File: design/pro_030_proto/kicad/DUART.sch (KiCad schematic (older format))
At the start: 1 part, among them U9 XR68C681CJTR-F-XR68C681

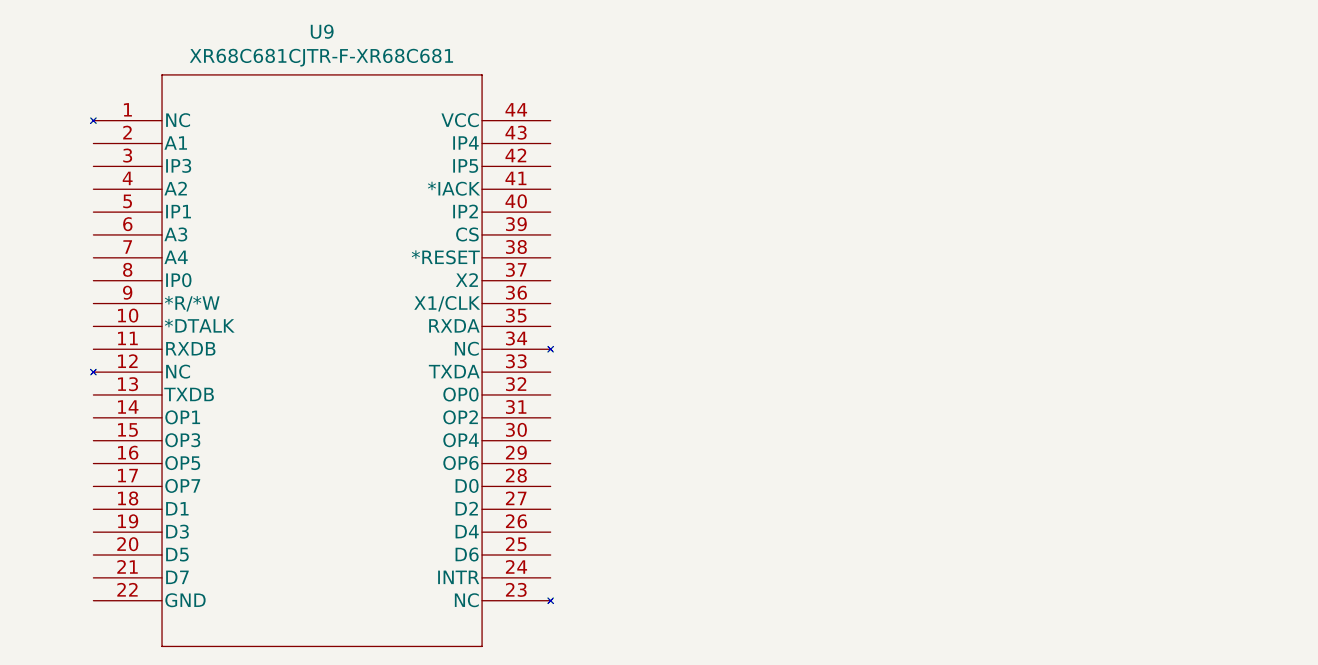
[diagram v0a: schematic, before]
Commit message: Add interrupt glue to schematic
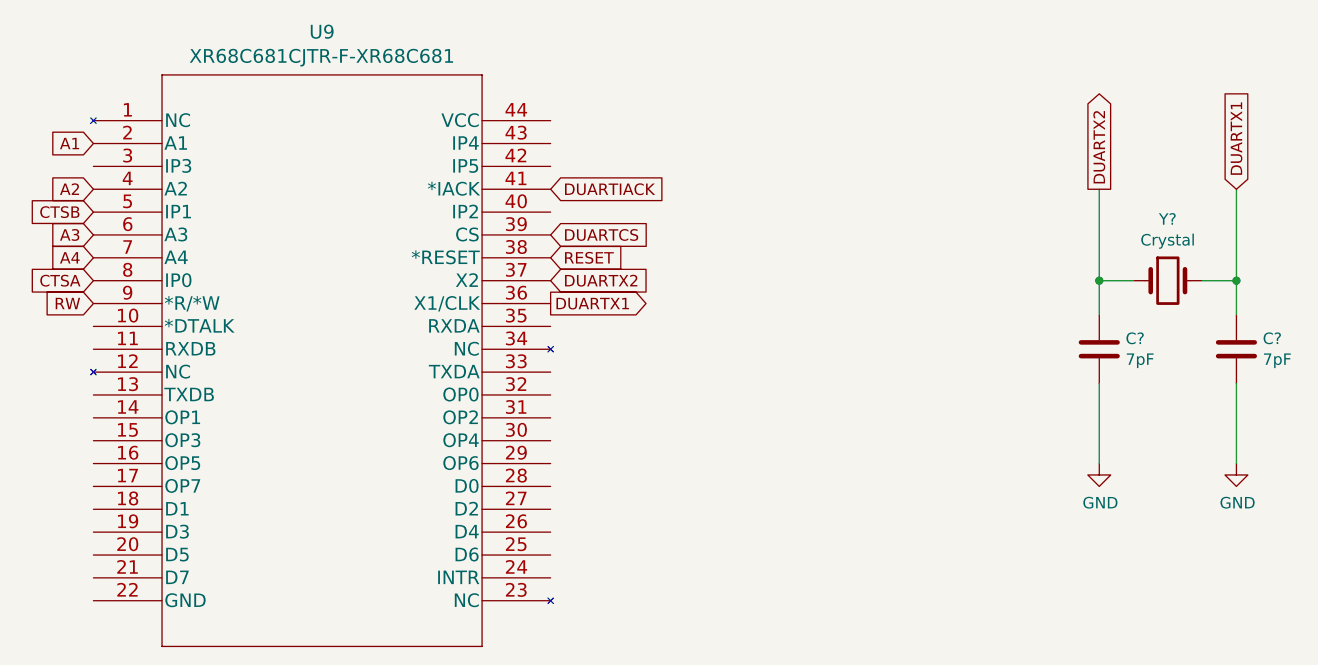
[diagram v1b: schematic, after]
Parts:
- added C? (x2): 7pF, Capacitor_THT:C_Rect_L4.0mm_W2.5mm_P2.50mm, symbol Device:C
- added Y?: Crystal, symbol Device:Crystal
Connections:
- net A1: now reaches U9.2 (A1)
- net DUARTX1: now reaches U9.36 (X1/CLK)
- net DUARTX1: now also C?.1, Y?.2
- net DUARTX2: now reaches U9.37 (X2)
- net DUARTX2: now also C?.1, Y?.1
- net RESET: now reaches U9.38 (*RESET)
- net DUARTCS: now reaches U9.39 (CS)
- net A2: now reaches U9.4 (A2)
- net DUARTIACK: now reaches U9.41 (*IACK)
- net CTSB: now reaches U9.5 (IP1)
- net A3: now reaches U9.6 (A3)
- net A4: now reaches U9.7 (A4)
- net CTSA: now reaches U9.8 (IP0)
- net RW: now reaches U9.9 (*R/*W)
- new net GND: C?.2, C?.2
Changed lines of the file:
@@
 $Descr A4 11693 8268
 encoding utf-8
-Sheet 5 7
+Sheet 5 8
 Title "rosco_m68k Pro (030) Prototype"
 Date "2021-07-16"
@@
 	1    0    0    -1
 $EndComp
+$Comp
+L Device:Crystal Y?
+U 1 1 60FCCD46
+P 7800 3450
+F 0 "Y?" H 7800 3718 50  0000 C CNN
+F 1 "Crystal" H 7800 3627 50  0000 C CNN
+F 2 "" H 7800 3450 50  0001 C CNN
+F 3 "~" H 7800 3450 50  0001 C CNN
+	1    7800 3450
+	1    0    0    -1
+$EndComp
+Text GLabel 5100 3450 2    50   Input ~ 0
+DUARTX2
+Text GLabel 5100 3550 2    50   Output ~ 0
+DUARTX1
+Text GLabel 7500 3050 1    50   Output ~ 0
+DUARTX2
+Text GLabel 8100 3050 1    50   Input ~ 0
+DUARTX1
+Wire Wire Line
+	7650 3450 7500 3450
+Wire Wire Line
+	7500 3450 7500 3050
+Wire Wire Line
+	7950 3450 8100 3450
+Wire Wire Line
+	8100 3450 8100 3050
+$Comp
+L Device:C C?
+U 1 1 60FD6D0D
+P 7500 3750
+AR Path="/60EC67C5/60FD6D0D" Ref="C?"  Part="1"
+AR Path="/60FBD3A8/60FD6D0D" Ref="C?"  Part="1"
+F 0 "C?" H 7615 3796 50  0000 L CNN
+F 1 "7pF" H 7615 3705 50  0000 L CNN
+F 2 "Capacitor_THT:C_Rect_L4.0mm_W2.5mm_P2.50mm" H 7538 3600 50  0001 C CNN
+F 3 "~" H 7500 3750 50  0001 C CNN
+	1    7500 3750
+	1    0    0    -1
+$EndComp
+$Comp
+L Device:C C?
+U 1 1 60FD71CD
+P 8100 3750
+AR Path="/60EC67C5/60FD71CD" Ref="C?"  Part="1"
+AR Path="/60FBD3A8/60FD71CD" Ref="C?"  Part="1"
+F 0 "C?" H 8215 3796 50  0000 L CNN
+F 1 "7pF" H 8215 3705 50  0000 L CNN
+F 2 "Capacitor_THT:C_Rect_L4.0mm_W2.5mm_P2.50mm" H 8138 3600 50  0001 C CNN
+F 3 "~" H 8100 3750 50  0001 C CNN
+	1    8100 3750
+	1    0    0    -1
+$EndComp
+Wire Wire Line
+	7500 3450 7500 3600
+Connection ~ 7500 3450
+Wire Wire Line
+	8100 3450 8100 3600
+Connection ~ 8100 3450
+$Comp
+L power:GND #PWR?
+U 1 1 60FD7528
+P 7500 4250
+F 0 "#PWR?" H 7500 4000 50  0001 C CNN
+F 1 "GND" H 7505 4077 50  0000 C CNN
+F 2 "" H 7500 4250 50  0001 C CNN
+F 3 "" H 7500 4250 50  0001 C CNN
+	1    7500 4250
+	1    0    0    -1
+$EndComp
+$Comp
+L power:GND #PWR?
+U 1 1 60FD7E93
+P 8100 4250
+F 0 "#PWR?" H 8100 4000 50  0001 C CNN
+F 1 "GND" H 8105 4077 50  0000 C CNN
+F 2 "" H 8100 4250 50  0001 C CNN
+F 3 "" H 8100 4250 50  0001 C CNN
+	1    8100 4250
+	1    0    0    -1
+$EndComp
+Wire Wire Line
+	7500 3900 7500 4250
+Wire Wire Line
+	8100 3900 8100 4250
+Text GLabel 5100 3350 2    50   Input ~ 0
+RESET
+Text GLabel 5100 3250 2    50   Input ~ 0
+DUARTCS
+Text GLabel 5100 3050 2    50   Input ~ 0
+DUARTIACK
+Text GLabel 3100 3450 0    50   Input ~ 0
+CTSA
+Text GLabel 3100 3150 0    50   Input ~ 0
+CTSB
+Text GLabel 3100 2850 0    50   Input ~ 0
+A1
+Text GLabel 3100 3050 0    50   Input ~ 0
+A2
+Text GLabel 3100 3250 0    50   Input ~ 0
+A3
+Text GLabel 3100 3350 0    50   Input ~ 0
+A4
+Text GLabel 3100 3550 0    50   Input ~ 0
+RW
 $EndSCHEMATC

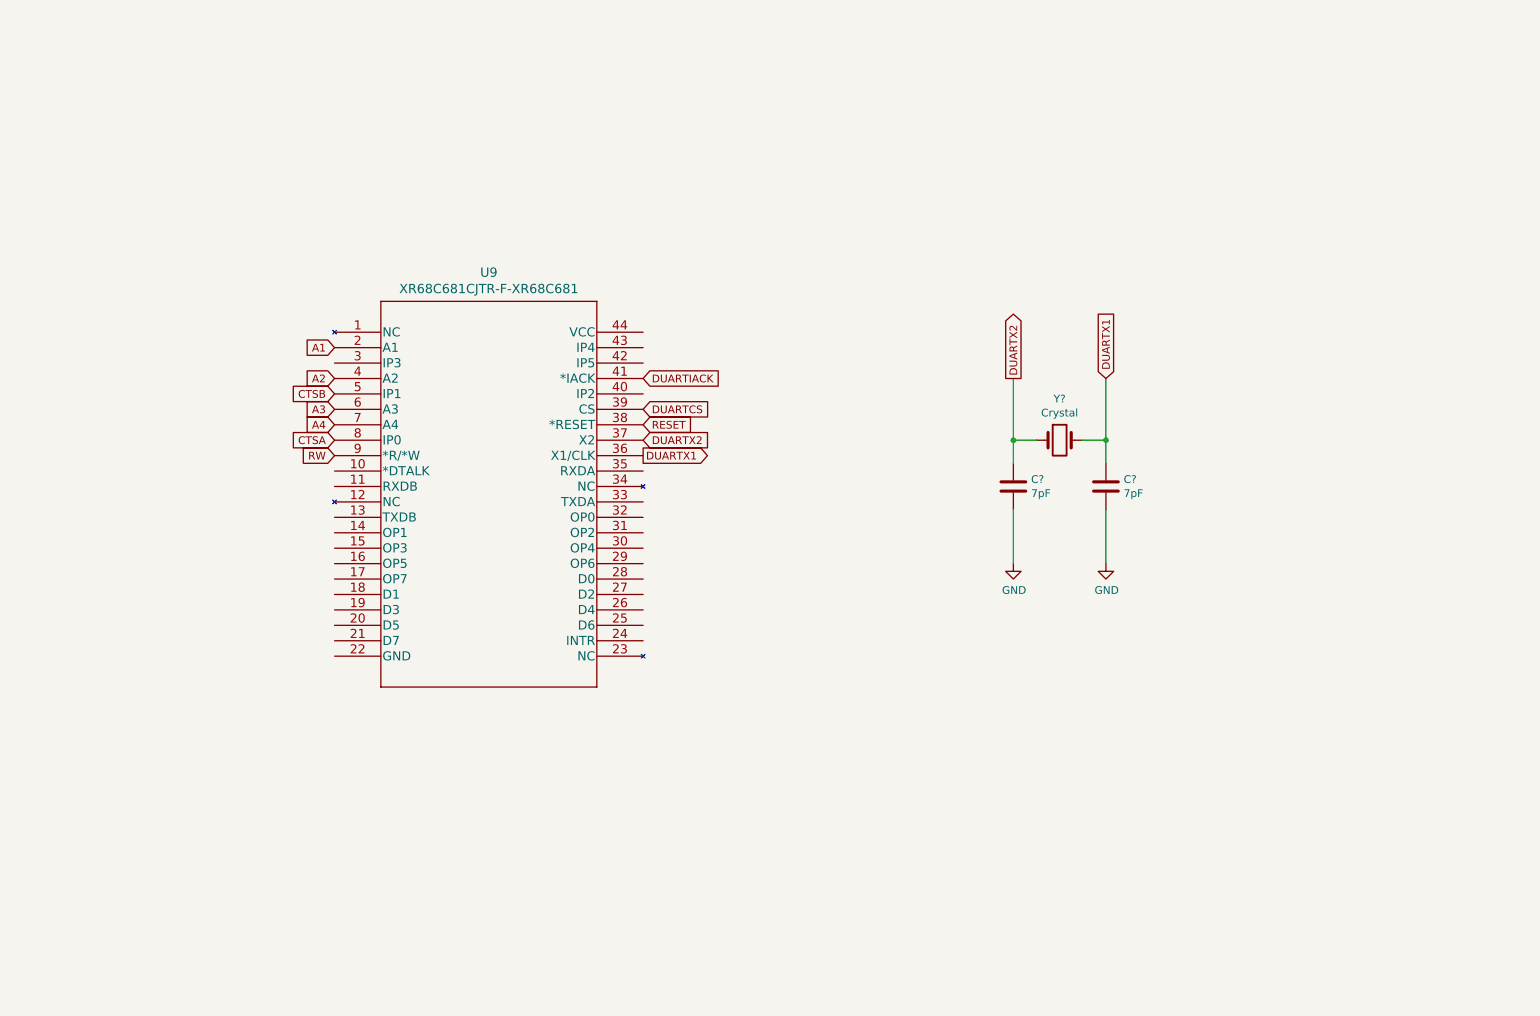
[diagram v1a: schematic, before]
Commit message: Largeish changeset:
* Added (first-cut) glue for DTACK generation
* Fix mem selects to use new DTACK generation
* Add missing footprints for Kicad
* Add POWER and TESTPOINTS schematics
* Update footprints across the board to allow error-free PCB import
* Pull all components (so far) into PCB
* Fix MC68030RC footprint (missing pads)
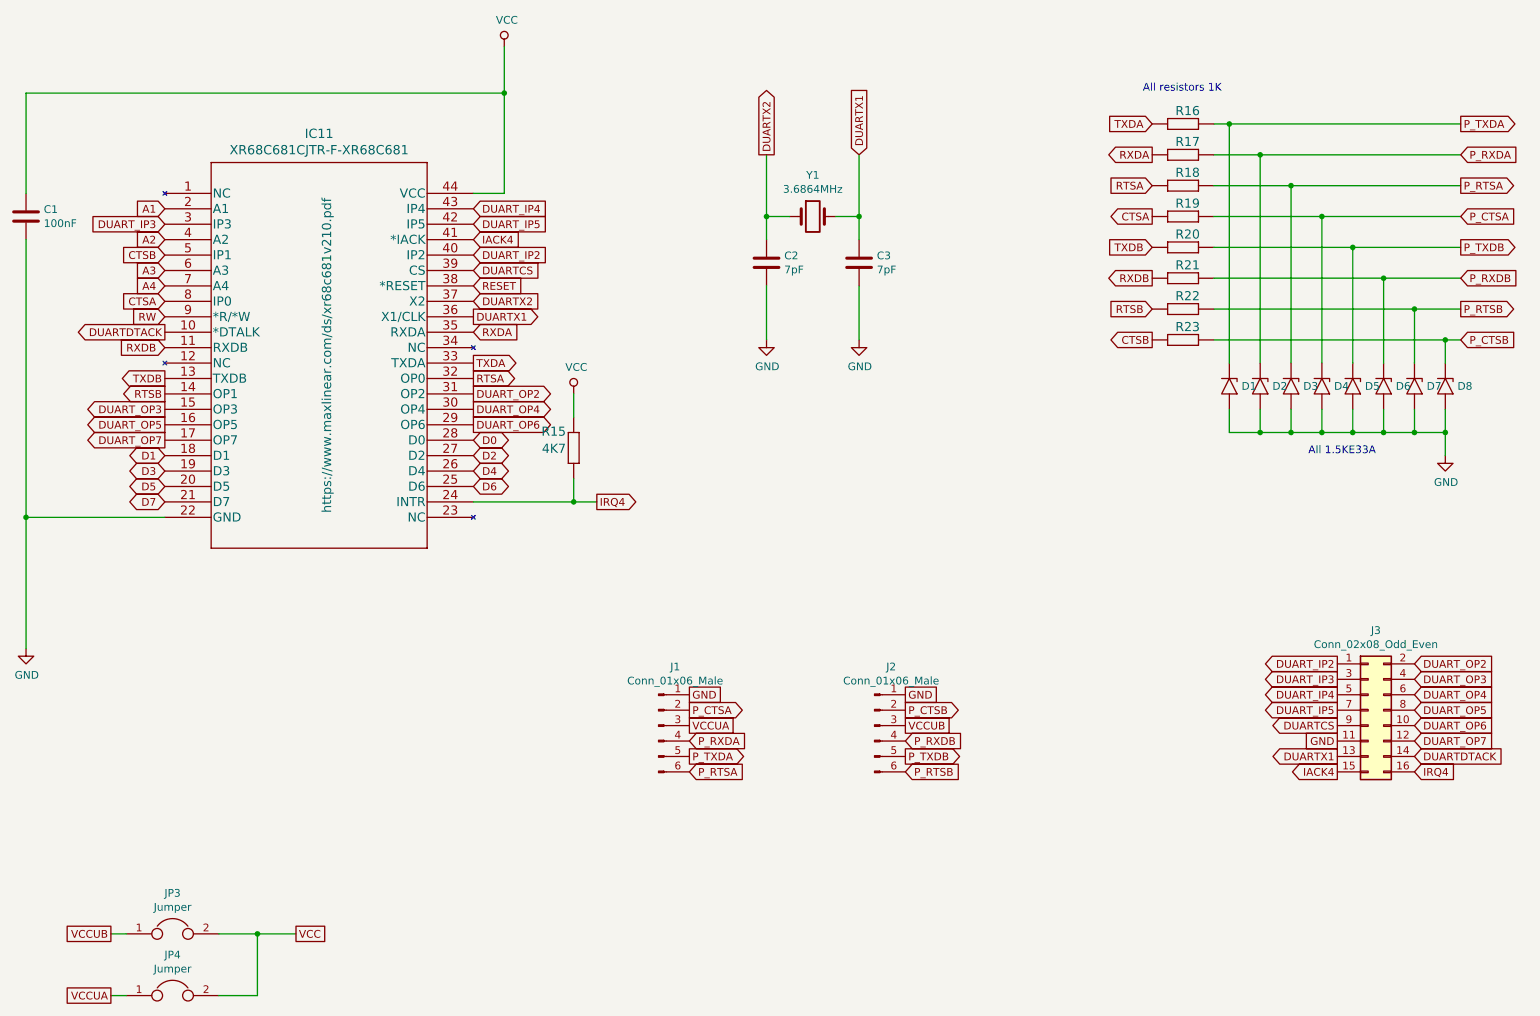
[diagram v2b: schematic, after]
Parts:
- added C1: 100nF, Capacitor_THT:C_Rect_L4.0mm_W2.5mm_P2.50mm, symbol Device:C
- added D1, D2, D3, D4, D5, D6, D7, D8: 1.5KE33A, Diode_THT:D_DO-201AE_P15.24mm_Horizontal, symbol Diode:1.5KExxA
- added J1, J2: Conn_01x06_Male, Connector_PinHeader_2.54mm:PinHeader_1x06_P2.54mm_Vertical, symbol Connector:Conn_01x06_Male
- added J3: Conn_02x08_Odd_Even, Connector_PinHeader_2.54mm:PinHeader_2x08_P2.54mm_Vertical, symbol Connector_Generic:Conn_02x08_Odd_Even
- added JP3, JP4: Jumper, rosco_m68k:pin-1X02, symbol Device:Jumper
- added R15: 4K7, rosco_m68k:R-0207_10, symbol rosco_m68k-eagle-import:R-EU_0207_10
- added R16, R17, R18, R19, R20, R21, R22, R23: 1K, rosco_m68k:R-0207_10, symbol rosco_m68k-eagle-import:R-EU_0207_10
- Y1: renamed from Y?; value Crystal -> 3.6864MHz; footprint (none) -> rosco_m68k:HC49_S
- gave numbers to parts that had none: 2
- renumbered U9 to IC11
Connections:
- net CTSA: now also R19.1
- net CTSB: now also R23.1
- net DUARTCS: now also J3.9 (Pin_9)
- net DUARTX1: now also J3.13 (Pin_13)
- net GND: now also IC11.22 (GND), C1.2, D1.2 (A2), D2.2 (A2), D3.2 (A2), D4.2 (A2), D5.2 (A2), D6.2 (A2), D7.2 (A2), D8.2 (A2), J1.1 (Pin_1), J2.1 (Pin_1), J3.11 (Pin_11)
- net DUARTDTACK: now reaches IC11.10 (*DTALK)
- net DUARTDTACK: now also J3.14 (Pin_14)
- net RXDB: now reaches IC11.11 (RXDB)
- net RXDB: now also R21.1
- net TXDB: now reaches IC11.13 (TXDB)
- net TXDB: now also R20.1
- net RTSB: now reaches IC11.14 (OP1)
- net RTSB: now also R22.1
- net DUART_OP3: now reaches IC11.15 (OP3)
- net DUART_OP3: now also J3.4 (Pin_4)
- net DUART_OP5: now reaches IC11.16 (OP5)
- net DUART_OP5: now also J3.8 (Pin_8)
- net DUART_OP7: now reaches IC11.17 (OP7)
- net DUART_OP7: now also J3.12 (Pin_12)
- net D1: now reaches IC11.18 (D1)
- net D3: now reaches IC11.19 (D3)
- net D5: now reaches IC11.20 (D5)
- net D7: now reaches IC11.21 (D7)
- net IRQ4: now reaches IC11.24 (INTR)
- net IRQ4: now also J3.16 (Pin_16), R15.1
- net D6: now reaches IC11.25 (D6)
- net D4: now reaches IC11.26 (D4)
- net D2: now reaches IC11.27 (D2)
- net D0: now reaches IC11.28 (D0)
- net DUART_OP6: now reaches IC11.29 (OP6)
- net DUART_OP6: now also J3.10 (Pin_10)
- net DUART_IP3: now reaches IC11.3 (IP3)
- net DUART_IP3: now also J3.3 (Pin_3)
- net DUART_OP4: now reaches IC11.30 (OP4)
- net DUART_OP4: now also J3.6 (Pin_6)
- net DUART_OP2: now reaches IC11.31 (OP2)
- net DUART_OP2: now also J3.2 (Pin_2)
- net RTSA: now reaches IC11.32 (OP0)
- net RTSA: now also R18.1
- net TXDA: now reaches IC11.33 (TXDA)
- net TXDA: now also R16.1
- net RXDA: now reaches IC11.35 (RXDA)
- net RXDA: now also R17.1
- net DUART_IP2: now reaches IC11.40 (IP2)
- net DUART_IP2: now also J3.1 (Pin_1)
- net DUART_IP5: now reaches IC11.42 (IP5)
- net DUART_IP5: now also J3.7 (Pin_7)
- net DUART_IP4: now reaches IC11.43 (IP4)
- net DUART_IP4: now also J3.5 (Pin_5)
- net VCC: now reaches IC11.44 (VCC)
- net VCC: now also C1.1, JP3.2, JP4.2, R15.2
- net DUARTIACK renamed IACK4
- net IACK4: now also J3.15 (Pin_15)
- new net P_CTSA: D4.1 (A1), J1.2 (Pin_2), R19.2
- new net P_CTSB: D8.1 (A1), J2.2 (Pin_2), R23.2
- new net P_RTSA: D3.1 (A1), J1.6 (Pin_6), R18.2
- new net P_RTSB: D7.1 (A1), J2.6 (Pin_6), R22.2
- new net P_RXDA: D2.1 (A1), J1.4 (Pin_4), R17.2
- new net P_RXDB: D6.1 (A1), J2.4 (Pin_4), R21.2
- new net P_TXDA: D1.1 (A1), J1.5 (Pin_5), R16.2
- new net P_TXDB: D5.1 (A1), J2.5 (Pin_5), R20.2
- new net VCCUA: J1.3 (Pin_3), JP4.1
- new net VCCUB: J2.3 (Pin_3), JP3.1
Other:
- note added: "All 1.5KE33A"
- note added: "All resistors 1K"
- moved on the sheet: C2, C3, IC11, Y1

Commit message: Interrupts + Xosera schematic, re-annotate
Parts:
- renumbered C2 to C10, C3 to C11, C1 to C9, IC11 to IC2
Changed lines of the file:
@@
 $Descr A4 11693 8268
 encoding utf-8
-Sheet 5 10
+Sheet 5 13
 Title "rosco_m68k Pro (030) Prototype"
 Date "2021-07-24"
@@
 $EndDescr
 $Comp
-L rosco_m68k:XR68C681CJTR-F-XR68C681 IC11
+L rosco_m68k:XR68C681CJTR-F-XR68C681 IC2
 U 1 1 60FBD731
 P 2000 1850
-F 0 "IC11" H 3000 2237 60  0000 C CNN
+F 0 "IC2" H 3000 2237 60  0000 C CNN
 F 1 "XR68C681CJTR-F-XR68C681" H 3000 2131 60  0000 C CNN
 F 2 "Package_LCC:PLCC-44_THT-Socket" H 3000 2090 60  0001 C CNN
@@
 P 5900 2300
 AR Path="/60EC67C5/60FD6D0D" Ref="C?"  Part="1"
-AR Path="/60FBD3A8/60FD6D0D" Ref="C2"  Part="1"
-F 0 "C2" H 6015 2346 50  0000 L CNN
+AR Path="/60FBD3A8/60FD6D0D" Ref="C10"  Part="1"
+F 0 "C10" H 6015 2346 50  0000 L CNN
 F 1 "7pF" H 6015 2255 50  0000 L CNN
 F 2 "Capacitor_THT:C_Rect_L4.0mm_W2.5mm_P2.50mm" H 5938 2150 50  0001 C CNN
@@
 P 6500 2300
 AR Path="/60EC67C5/60FD71CD" Ref="C?"  Part="1"
-AR Path="/60FBD3A8/60FD71CD" Ref="C3"  Part="1"
-F 0 "C3" H 6615 2346 50  0000 L CNN
+AR Path="/60FBD3A8/60FD71CD" Ref="C11"  Part="1"
+F 0 "C11" H 6615 2346 50  0000 L CNN
 F 1 "7pF" H 6615 2255 50  0000 L CNN
 F 2 "Capacitor_THT:C_Rect_L4.0mm_W2.5mm_P2.50mm" H 6538 2150 50  0001 C CNN
@@
 Connection ~ 6500 2000
 $Comp
-L power:GND #PWR0106
+L power:GND #PWR015
 U 1 1 60FD7528
 P 5900 2800
-F 0 "#PWR0106" H 5900 2550 50  0001 C CNN
+F 0 "#PWR015" H 5900 2550 50  0001 C CNN
 F 1 "GND" H 5905 2627 50  0000 C CNN
 F 2 "" H 5900 2800 50  0001 C CNN
@@
 $EndComp
 $Comp
-L power:GND #PWR0107
+L power:GND #PWR016
 U 1 1 60FD7E93
 P 6500 2800
-F 0 "#PWR0107" H 6500 2550 50  0001 C CNN
+F 0 "#PWR016" H 6500 2550 50  0001 C CNN
 F 1 "GND" H 6505 2627 50  0000 C CNN
 F 2 "" H 6500 2800 50  0001 C CNN
@@
 DUART_IP4
 $Comp
-L power:VCC #PWR0108
+L power:VCC #PWR013
 U 1 1 60FDD54E
 P 4200 900
-F 0 "#PWR0108" H 4200 750 50  0001 C CNN
+F 0 "#PWR013" H 4200 750 50  0001 C CNN
 F 1 "VCC" H 4217 1073 50  0000 C CNN
 F 2 "" H 4200 900 50  0001 C CNN
@@
 $EndComp
 $Comp
-L power:GND #PWR0109
+L power:GND #PWR012
 U 1 1 60FDD6E9
 P 1100 4800
-F 0 "#PWR0109" H 1100 4550 50  0001 C CNN
+F 0 "#PWR012" H 1100 4550 50  0001 C CNN
 F 1 "GND" H 1105 4627 50  0000 C CNN
 F 2 "" H 1100 4800 50  0001 C CNN
@@
 P 1100 2000
 AR Path="/60EC67C5/60FDE98A" Ref="C?"  Part="1"
-AR Path="/60FBD3A8/60FDE98A" Ref="C1"  Part="1"
-F 0 "C1" H 1215 2046 50  0000 L CNN
+AR Path="/60FBD3A8/60FDE98A" Ref="C9"  Part="1"
+F 0 "C9" H 1215 2046 50  0000 L CNN
 F 1 "100nF" H 1215 1955 50  0000 L CNN
 F 2 "Capacitor_THT:C_Rect_L4.0mm_W2.5mm_P2.50mm" H 1138 1850 50  0001 C CNN
@@
 RXDB
 $Comp
-L power:VCC #PWR0112
+L power:VCC #PWR014
 U 1 1 60FDAD2F
 P 4650 3150
-F 0 "#PWR0112" H 4650 3000 50  0001 C CNN
+F 0 "#PWR014" H 4650 3000 50  0001 C CNN
 F 1 "VCC" H 4667 3323 50  0000 C CNN
 F 2 "" H 4650 3150 50  0001 C CNN
@@
 	10100 2600 8800 2600
 $Comp
-L power:GND #PWR0113
+L power:GND #PWR017
 U 1 1 61071C44
 P 10300 3550
-F 0 "#PWR0113" H 10300 3300 50  0001 C CNN
+F 0 "#PWR017" H 10300 3300 50  0001 C CNN
 F 1 "GND" H 10305 3377 50  0000 C CNN
 F 2 "" H 10300 3550 50  0001 C CNN

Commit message: Big(ish) push on placement
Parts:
- JP3, JP4: footprint rosco_m68k:pin-1X02 -> Connector_PinHeader_2.54mm:PinHeader_1x02_P2.54mm_Vertical
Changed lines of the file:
@@
 F 0 "JP3" H 2050 6914 50  0000 C CNN
 F 1 "Jumper" H 2050 6823 50  0000 C CNN
-F 2 "rosco_m68k:pin-1X02" H 2050 6650 50  0001 C CNN
+F 2 "Connector_PinHeader_2.54mm:PinHeader_1x02_P2.54mm_Vertical" H 2050 6650 50  0001 C CNN
 F 3 "~" H 2050 6650 50  0001 C CNN
 	1    2050 6650
@@
 F 0 "JP4" H 2050 7314 50  0000 C CNN
 F 1 "Jumper" H 2050 7223 50  0000 C CNN
-F 2 "rosco_m68k:pin-1X02" H 2050 7050 50  0001 C CNN
+F 2 "Connector_PinHeader_2.54mm:PinHeader_1x02_P2.54mm_Vertical" H 2050 7050 50  0001 C CNN
 F 3 "~" H 2050 7050 50  0001 C CNN
 	1    2050 7050
